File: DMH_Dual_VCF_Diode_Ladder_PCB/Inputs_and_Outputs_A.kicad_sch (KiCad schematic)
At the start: 8 parts, among them J1 TS_Jack_6.35mm_Sw, J2 TS_Jack_6.35mm_Sw, J200 IDC_02x05, J3 TS_Jack_6.35mm_Sw, J4 TS_Jack_6.35mm_Sw, J5 TS_Jack_6.35mm_Sw, J50 Conn_01x06, J60 Conn_01x06

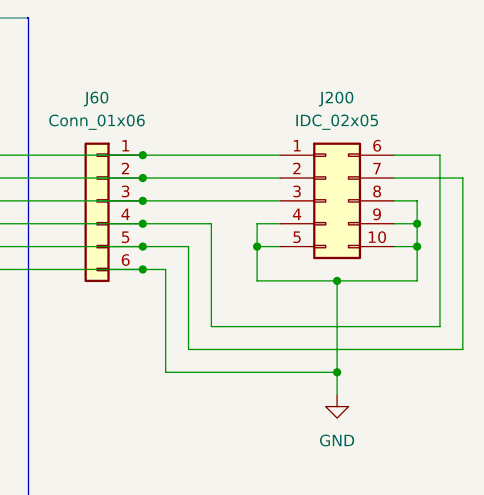
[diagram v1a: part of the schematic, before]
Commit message: Concluded core and resonance circuits design
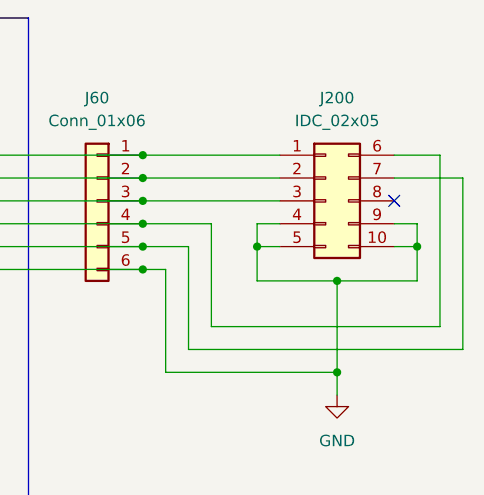
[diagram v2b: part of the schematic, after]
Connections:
- net GND: no longer J200.8 (Pin_8)
- no-connect marks 0 -> 1
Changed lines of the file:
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@@
-	)
-	(junction
-		(at 162.56 48.26)
-		(diameter 0)
-		(color 0 0 0 0)
 	)
 	(junction
@@
 		(color 0 0 0 0)
 	)
+	(no_connect
+		(at 160.02 45.72)
+	)
 	(wire
 		(pts
@@
 	(wire
 		(pts
-			(xy 160.02 45.72) (xy 162.56 45.72)
-		)
-		(stroke
-			(width 0)
-			(type default)
-		)
-	)
-	(wire
-		(pts
 			(xy 111.76 139.7) (xy 111.76 116.84)
 		)
@@
 		)
 		(stroke
-			(width 0)
-			(type default)
-		)
-	)
-	(wire
-		(pts
-			(xy 162.56 45.72) (xy 162.56 48.26)
-		)
-		(stroke

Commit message: Finished designing circuit
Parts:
- added SW4: SW_SPDT_321, SynthStuff:Toggle_Switch_THT, symbol Switch:SW_SPDT_321
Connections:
- net Input Jack: now also SW4.3 (A)
- net Output Jack: now also SW4.1 (C)
- new net Feed Switch: SW4.2 (B)
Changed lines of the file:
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@@
+	)
+	(junction
+		(at 148.59 106.68)
+		(diameter 0)
+		(color 0 0 0 0)
+	)
+	(junction
+		(at 144.78 116.84)
+		(diameter 0)
+		(color 0 0 0 0)
 	)
 	(junction
@@
 	(wire
 		(pts
+			(xy 144.78 116.84) (xy 152.4 116.84)
+		)
+		(stroke
+			(width 0)
+			(type default)
+		)
+	)
+	(wire
+		(pts
 			(xy 63.5 137.16) (xy 114.3 137.16)
 		)
@@
 	(wire
 		(pts
+			(xy 144.78 135.89) (xy 144.78 116.84)
+		)
+		(stroke
+			(width 0)
+			(type default)
+		)
+	)
+	(wire
+		(pts
 			(xy 139.7 119.38) (xy 139.7 121.92)
 		)
@@
 	(wire
 		(pts
-			(xy 132.08 116.84) (xy 152.4 116.84)
+			(xy 132.08 116.84) (xy 144.78 116.84)
 		)
 		(stroke
@@
 	(wire
 		(pts
+			(xy 166.37 135.89) (xy 144.78 135.89)
+		)
+		(stroke
+			(width 0)
+			(type default)
+		)
+	)
+	(wire
+		(pts
 			(xy 132.08 111.76) (xy 152.4 111.76)
 		)
@@
 	(wire
 		(pts
+			(xy 148.59 130.81) (xy 148.59 106.68)
+		)
+		(stroke
+			(width 0)
+			(type default)
+		)
+	)
+	(wire
+		(pts
 			(xy 132.08 43.18) (xy 147.32 43.18)
 		)
@@
 	(wire
 		(pts
-			(xy 132.08 106.68) (xy 152.4 106.68)
+			(xy 132.08 106.68) (xy 148.59 106.68)
 		)
 		(stroke
@@
 	(wire
 		(pts
+			(xy 166.37 130.81) (xy 148.59 130.81)
+		)
+		(stroke
+			(width 0)
+			(type default)
+		)
+	)
+	(wire
+		(pts
 			(xy 160.02 43.18) (xy 167.64 43.18)
 		)
@@
 	(wire
 		(pts
+			(xy 176.53 133.35) (xy 184.15 133.35)
+		)
+		(stroke
+			(width 0)
+			(type default)
+		)
+	)
+	(wire
+		(pts
 			(xy 55.88 38.1) (xy 99.06 38.1)
 		)
@@
 		(pts
 			(xy 63.5 53.34) (xy 63.5 60.96)
+		)
+		(stroke
+			(width 0)
+			(type default)
+		)
+	)
+	(wire
+		(pts
+			(xy 148.59 106.68) (xy 152.4 106.68)
 		)
 		(stroke
@@
 		(shape output)
 		(at 152.4 111.76 0)
+		(fields_autoplaced yes)
+		(effects
+			(font
+				(size 1.27 1.27)
+			)
+			(justify left)
+		)
+	)
+	(hierarchical_label "Feed Switch"
+		(shape output)
+		(at 184.15 133.35 0)
 		(fields_autoplaced yes)
 		(effects
@@
 					(unit 1)
 				)
+			)
+		)
+	)
+	(symbol
+		(lib_id "Switch:SW_SPDT_321")
+		(at 171.45 133.35 0)
+		(mirror y)
+		(unit 1)
+		(exclude_from_sim no)
+		(in_bom yes)
+		(on_board yes)
+		(dnp no)
+		(property "Reference" "SW4"
+			(at 171.45 124.46 0)
+			(effects
+				(font
+					(size 1.27 1.27)
+				)
+			)
+		)
+		(property "Value" "SW_SPDT_321"
+			(at 171.45 127 0)
+			(effects
+				(font
+					(size 1.27 1.27)
+				)
+			)
+		)
+		(property "Footprint" "SynthStuff:Toggle_Switch_THT"
+			(at 171.45 143.51 0)
+			(effects
+				(font
+					(size 1.27 1.27)
+				)
+				(hide yes)
+			)
+		)
+		(property "Datasheet" "~"
+			(at 171.45 140.97 0)
+			(effects
+				(font
+					(size 1.27 1.27)
+				)
+				(hide yes)
+			)
+		)
+		(property "Description" "Switch, single pole double throw"
+			(at 171.45 133.35 0)
+			(effects
+				(font
+					(size 1.27 1.27)
+				)
+				(hide yes)
+			)
+		)
+		(property "Function" "Feed"
+			(at 171.45 138.938 0)
+			(effects
+				(font
+					(size 1.27 1.27)
+					(thickness 0.254)
+					(bold yes)
+					(italic yes)
+				)
+			)
+		)
+		(pin "1"
+		)
+		(pin "3"
+		)
+		(pin "2"
+		)
+		(instances
+			(project "DMH_Dual_VCF_Diode_Ladder_PCB"
+				(path "/58f4306d-5387-4983-bb08-41a2313fd315/ce3fef8b-9f1d-4178-b50b-4a046c030679"
+					(reference "SW4")
+					(unit 1)
+				)

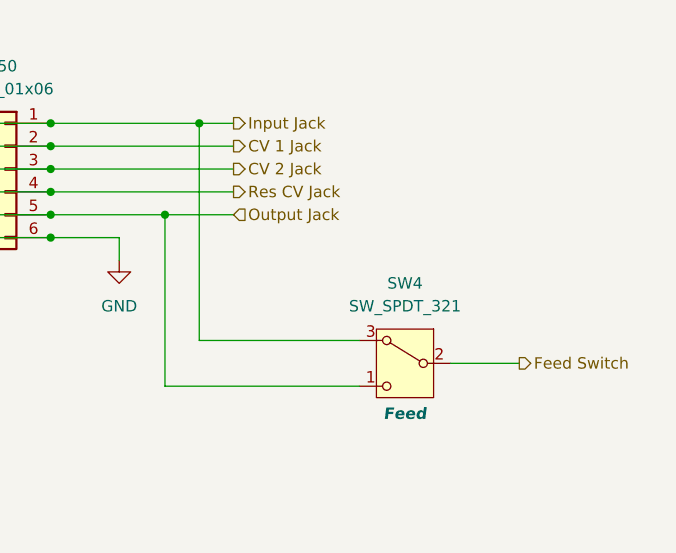
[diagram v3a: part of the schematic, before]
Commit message: Reannotated whole schematic
OpAmp annotation is still tentative.
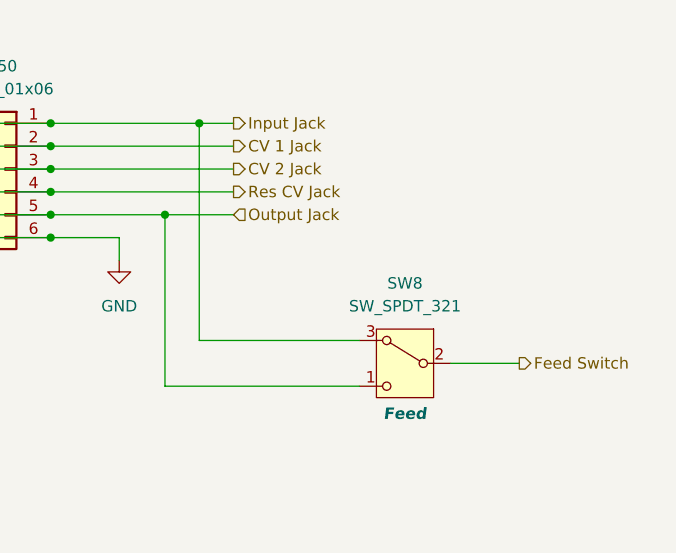
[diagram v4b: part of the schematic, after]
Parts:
- renumbered SW4 to SW8
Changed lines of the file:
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@@
 		(on_board yes)
 		(dnp no)
-		(property "Reference" "SW4"
+		(property "Reference" "SW8"
 			(at 171.45 124.46 0)
 			(effects
@@
 			(project "DMH_Dual_VCF_Diode_Ladder_PCB"
 				(path "/58f4306d-5387-4983-bb08-41a2313fd315/ce3fef8b-9f1d-4178-b50b-4a046c030679"
-					(reference "SW4")
+					(reference "SW8")
 					(unit 1)
 				)

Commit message: Updated switches symbols and fps
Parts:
- SW8: footprint SynthStuff:Toggle_Switch_THT -> SynthStuff:Toggle_Switch_TE
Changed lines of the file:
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@@
 			)
 		)
-		(property "Footprint" "SynthStuff:Toggle_Switch_THT"
+		(property "Footprint" "SynthStuff:Toggle_Switch_TE"
 			(at 171.45 143.51 0)
 			(effects

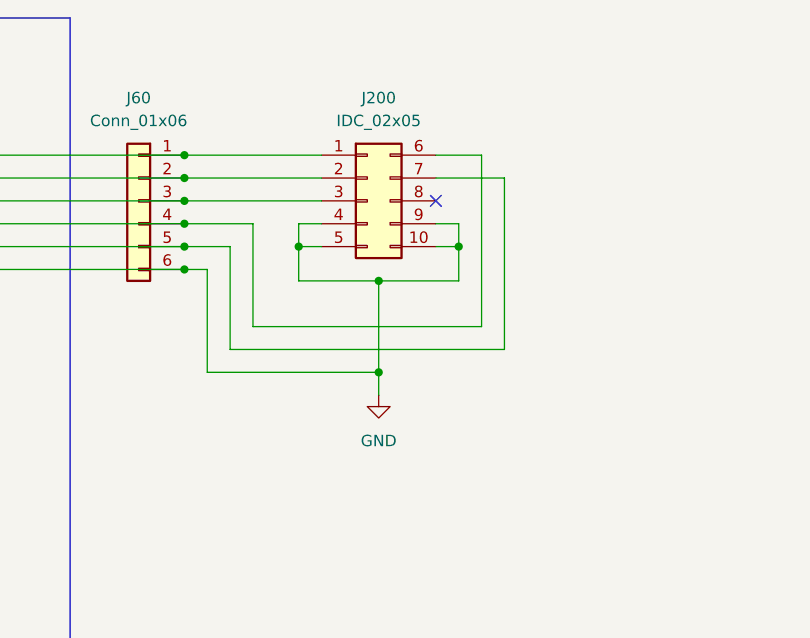
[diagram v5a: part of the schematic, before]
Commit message: Placed ICs and prepared passives
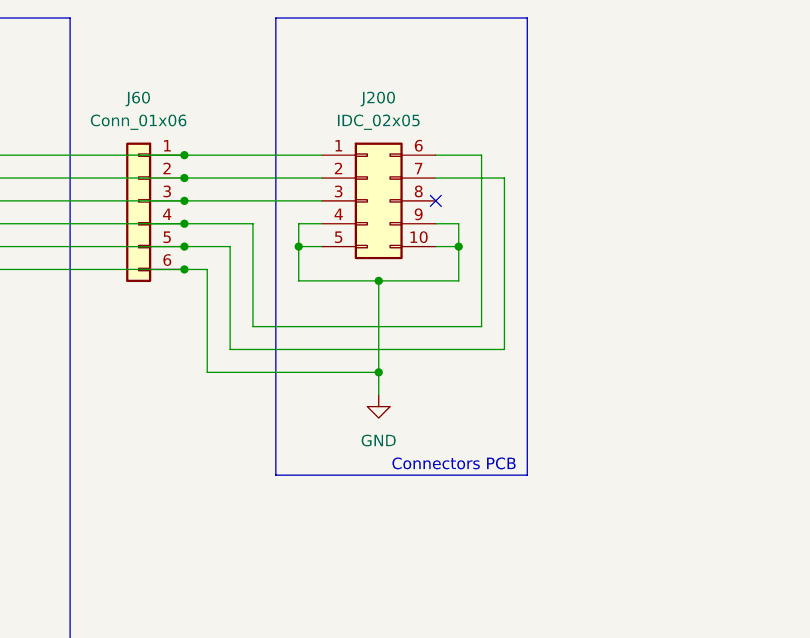
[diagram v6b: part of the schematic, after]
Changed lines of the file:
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@@
+		)
+	)
+	(rectangle
+		(start 142.24 25.4)
+		(end 170.18 76.2)
+		(stroke
+			(width 0)
+			(type default)
+		)
+		(fill
+			(type none)
+		)
+	)
+	(text "Connectors PCB"
+		(exclude_from_sim no)
+		(at 162.052 75.184 0)
+		(effects
+			(font
+				(size 1.27 1.27)
+			)
 		)
 	)
@@
 		(exclude_from_sim no)
 		(in_bom yes)
-		(on_board yes)
-		(dnp no)
-		(fields_autoplaced yes)
+		(on_board no)
+		(dnp no)
+		(fields_autoplaced yes)

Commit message: Finished routing
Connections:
- net GND: no longer J60.6 (Pin_6)
- net at J1.TN, J200.1 (Pin_1): no longer J60.1 (Pin_1)
- net at J2.TN, J200.2 (Pin_2): no longer J60.2 (Pin_2)
- net at J200.3 (Pin_3), J3.TN: no longer J60.3 (Pin_3)
- net at J200.6 (Pin_6), J4.TN: no longer J60.4 (Pin_4)
- net at J200.7 (Pin_7), J5.TN: no longer J60.5 (Pin_5)
- no-connect marks 1 -> 7
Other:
- moved on the sheet: J60
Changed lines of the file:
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@@
-	)
-	(junction
-		(at 132.08 43.18)
-		(diameter 0)
-		(color 0 0 0 0)
 	)
 	(junction
@@
 	)
 	(junction
-		(at 132.08 48.26)
-		(diameter 0)
-		(color 0 0 0 0)
-	)
-	(junction
 		(at 132.08 106.68)
 		(diameter 0)
@@
 	)
 	(junction
-		(at 132.08 53.34)
-		(diameter 0)
-		(color 0 0 0 0)
-	)
-	(junction
 		(at 144.78 50.8)
 		(diameter 0)
@@
 	)
 	(junction
-		(at 132.08 50.8)
-		(diameter 0)
-		(color 0 0 0 0)
-	)
-	(junction
-		(at 132.08 40.64)
-		(diameter 0)
-		(color 0 0 0 0)
-	)
-	(junction
 		(at 63.5 111.76)
 		(diameter 0)
@@
 	)
 	(junction
-		(at 132.08 45.72)
-		(diameter 0)
-		(color 0 0 0 0)
-	)
-	(junction
 		(at 153.67 54.61)
 		(diameter 0)
@@
 		(diameter 0)
 		(color 0 0 0 0)
+	)
+	(no_connect
+		(at 132.08 76.2)
+	)
+	(no_connect
+		(at 132.08 71.12)
+	)
+	(no_connect
+		(at 132.08 68.58)
+	)
+	(no_connect
+		(at 132.08 63.5)
 	)
 	(no_connect
 		(at 160.02 45.72)
 	)
+	(no_connect
+		(at 132.08 73.66)
+	)
+	(no_connect
+		(at 132.08 66.04)
+	)
 	(wire
 		(pts
@@
 	(wire
 		(pts
-			(xy 132.08 53.34) (xy 134.62 53.34)
+			(xy 63.5 53.34) (xy 134.62 53.34)
 		)
 		(stroke
@@
 	(wire
 		(pts
-			(xy 101.6 43.18) (xy 132.08 43.18)
-		)
-		(stroke
-			(width 0)
-			(type default)
-		)
-	)
-	(wire
-		(pts
 			(xy 114.3 137.16) (xy 114.3 119.38)
 		)
@@
 	(wire
 		(pts
-			(xy 132.08 45.72) (xy 147.32 45.72)
+			(xy 104.14 45.72) (xy 147.32 45.72)
 		)
 		(stroke
@@
 	(wire
 		(pts
-			(xy 132.08 40.64) (xy 147.32 40.64)
+			(xy 55.88 40.64) (xy 147.32 40.64)
 		)
 		(stroke
@@
 	(wire
 		(pts
-			(xy 104.14 45.72) (xy 132.08 45.72)
-		)
-		(stroke
-			(width 0)
-			(type default)
-		)
-	)
-	(wire
-		(pts
 			(xy 162.56 50.8) (xy 162.56 48.26)
 		)
@@
 	(wire
 		(pts
-			(xy 55.88 40.64) (xy 132.08 40.64)
-		)
-		(stroke
-			(width 0)
-			(type default)
-		)
-	)
-	(wire
-		(pts
 			(xy 132.08 119.38) (xy 139.7 119.38)
 		)
@@
 	(wire
 		(pts
-			(xy 132.08 43.18) (xy 147.32 43.18)
+			(xy 101.6 43.18) (xy 147.32 43.18)
 		)
 		(stroke
@@
 	(wire
 		(pts
-			(xy 63.5 53.34) (xy 132.08 53.34)
-		)
-		(stroke
-			(width 0)
-			(type default)
-		)
-	)
-	(wire
-		(pts
 			(xy 153.67 54.61) (xy 153.67 64.77)
 		)
@@
 	(wire
 		(pts
-			(xy 137.16 50.8) (xy 132.08 50.8)
-		)
-		(stroke
-			(width 0)
-			(type default)
-		)
-	)
-	(wire
-		(pts
 			(xy 147.32 48.26) (xy 144.78 48.26)
 		)
@@
 	(wire
 		(pts
-			(xy 106.68 48.26) (xy 132.08 48.26)
+			(xy 106.68 48.26) (xy 139.7 48.26)
 		)
 		(stroke
@@
 	(wire
 		(pts
-			(xy 109.22 50.8) (xy 132.08 50.8)
+			(xy 109.22 50.8) (xy 137.16 50.8)
 		)
 		(stroke
@@
 		(pts
 			(xy 148.59 106.68) (xy 152.4 106.68)
-		)
-		(stroke
-			(width 0)
-			(type default)
-		)
-	)
-	(wire
-		(pts
-			(xy 132.08 48.26) (xy 139.7 48.26)
 		)
 		(stroke
@@
 	(symbol
 		(lib_id "Connector_Generic:Conn_01x06")
-		(at 127 45.72 0)
+		(at 127 68.58 0)
 		(mirror y)
 		(unit 1)
@@
 		(fields_autoplaced yes)
 		(property "Reference" "J60"
-			(at 127 34.29 0)
+			(at 127 57.15 0)
 			(effects
 				(font
@@
 		)
 		(property "Value" "Conn_01x06"
-			(at 127 36.83 0)
+			(at 127 59.69 0)
 			(effects
 				(font
@@
 		)
 		(property "Footprint" "Connector_PinSocket_2.54mm:PinSocket_1x06_P2.54mm_Vertical"
-			(at 127 45.72 0)
+			(at 127 68.58 0)
 			(effects
 				(font
@@
 		)
 		(property "Datasheet" "~"
-			(at 127 45.72 0)
+			(at 127 68.58 0)
 			(effects
 				(font
@@
 		)
 		(property "Description" "Generic connector, single row, 01x06, script generated (kicad-library-utils/schlib/autogen/connector/)"
-			(at 127 45.72 0)
+			(at 127 68.58 0)
 			(effects
 				(font
